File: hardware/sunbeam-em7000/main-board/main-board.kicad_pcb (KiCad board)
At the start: 4 copper layers, 131 x 125 mm, 456 parts, among them J101 TAB1_LINE1, J102 TAB2_LINE_IN, J103 TAB3_NEUTRAL_IN, J106 TAB6_COFVALVE, J107 TAB7_COFFPUMP, J108 TAB8_STEAMPUMP, J109 TAB9_HOTVALVE, J110 WB_RET, J401 SWD, J402 USB_PANEL, J501 TEMP_C, J502 TEMP_S, J503 TEMP_W, J520 FLOW, J521 STM_D, J522 BREW_D, J523 SPARE_A, J524 BREW_A, J525 SPARE_AN2_H, J570 CURR1_H, J571 CURR2_H, J620 PT1_H, J622 PT1_2W_P, J623 PT1_23W_N, J625 PT2_H, J627 PT2_2W_P, J628 PT2_23W_N, J630 WT1_H, J635 WT2_H, J761 WB_LV10, J791 SP2, J821 CON2, J861 KNOB, J862 REED, K201 HF115F-Q/005-1H, K731 HF32FA-G/005-HSL1, K741 HF32FA-G/005-HSL1, Q201 NX3008NBK, Q202 NX3008NBK, Q701 AO3400A, Q711 AO3400A, Q731 AO3400A, Q741 AO3400A, Q761 AO3400A, Q771 AO3400A, Q821 AO3400A, Q822 AO3401A, Q823 AO3400A, Q824 AO3400A, SW401 RESET, T701 BTA204S-600B, T711 BTA204S-600B, U201 74AHCT1G17, U301 IRM-20-5, U302 LT1963AEST-3.3#TRPBF, U401 STM32H743VIT6, U402 TLV803SDBZR, U520 SN74LVC1G17, U601 AMC131M02, U602 LTV-814S-TA1-A, U620 MAX31865ATP+, U621 MAX31865ATP+, U630 HX711, U631 HX711, U701 MOC3052SVM, U711 MOC3052SVM, U791 SN74HCT541PWR, Y401 8 MHz, Y402 32.768 kHz, Y601 8.000MHz

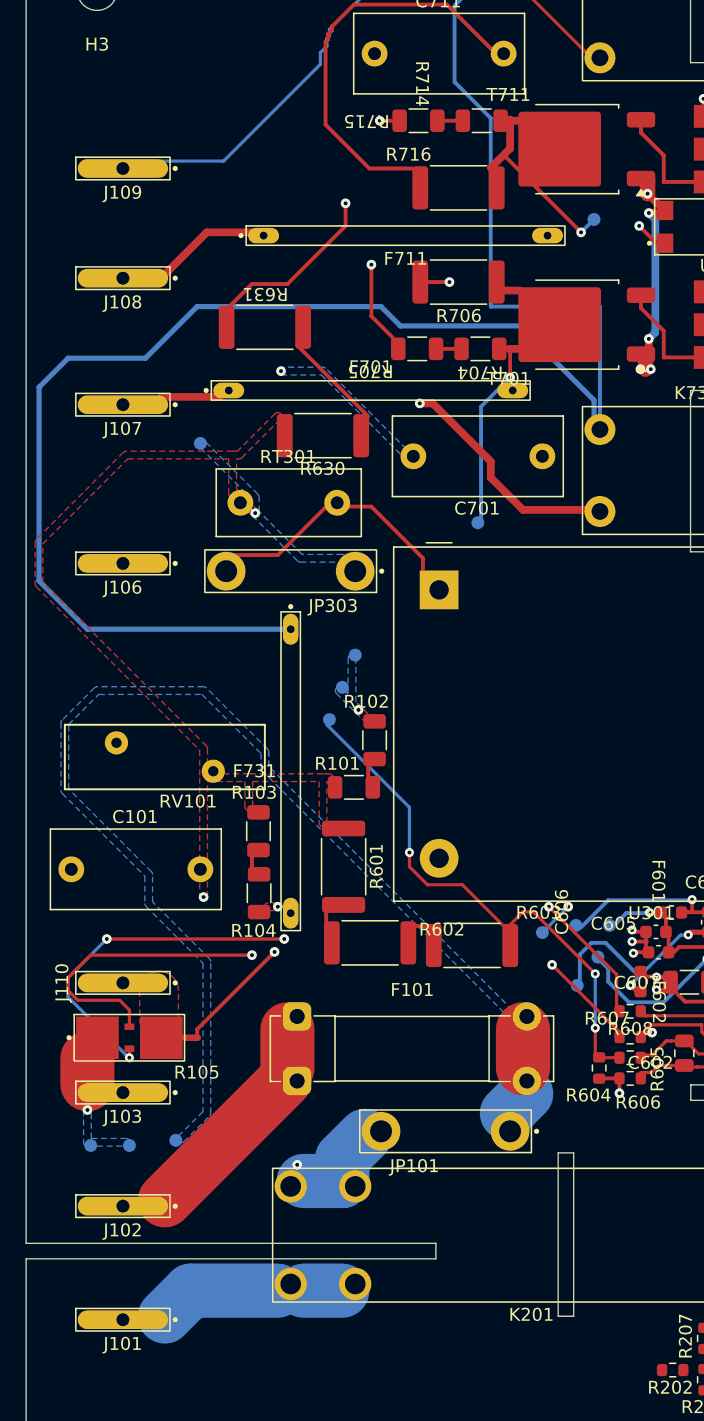
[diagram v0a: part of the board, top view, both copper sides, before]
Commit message: main-board: connect every mains pad the pours left open and fix the mains copper defects found by the early review [SOL-HW-MAIN-BOARD-PROVEN-AND-LAID-OUT.C7]
The NEUTRAL trunk link R105.4-J110.1 (a pour that filled to nothing) is two 3.0 mm tracks with two vias; the triac neutral island, LINE R101/R103, NEUTRAL R102/R104/F731, F711 and the test pads TP101, TP106, TP108 are joined by tracks; LINE1 no longer reaches past the mains region edge; T701 and T711 stand on F.Cu and B.Cu lands; TP105 and TP107 have vias of their own. TP102 stays unconnected (no routable path).

Co-Authored-By: Claude Sonnet 5.5 <noreply@anthropic.com>
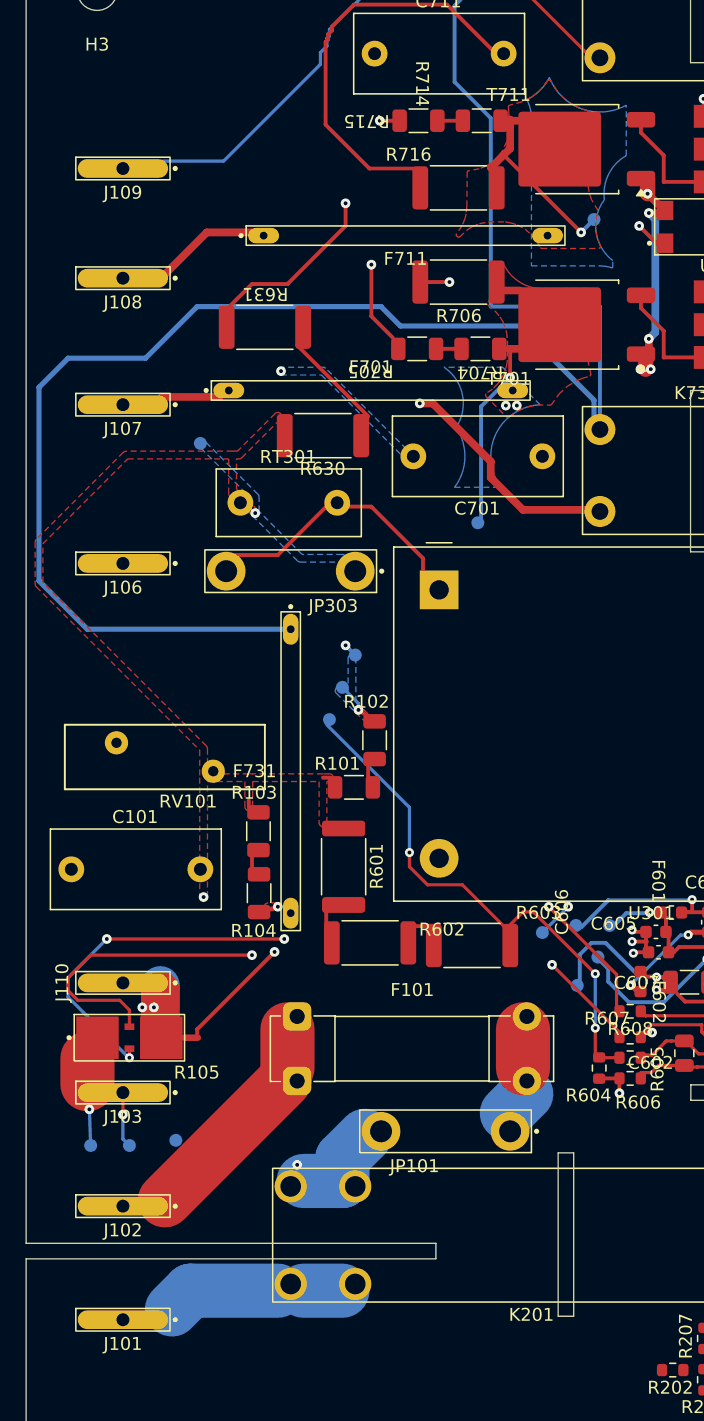
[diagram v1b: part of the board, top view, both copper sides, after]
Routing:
- net /NEUTRAL: track 14.9 -> 46.3 mm, vias 8 -> 11
- net /Mains entry and load feed/NEUTRAL_IN: track 2.00 -> 8.61 mm, vias 1 -> 2
- net /Mains entry and load feed/LINE_IN: track 16.1 -> 21.1 mm
- net /LINE: track 7.22 -> 9.96 mm
- net /LINE1: track 12.6 -> 11.8 mm
- net /Pump drives/PUMP_C_MT2: vias 1 -> 3
- added copper zone on B.Cu, net /Pump drives/PUMP_C_MT2
- added copper zone on F.Cu, net /Pump drives/PUMP_C_MT2
- added copper zone on B.Cu, net /Pump drives/PUMP_S_MT2
- added copper zone on F.Cu, net /Pump drives/PUMP_S_MT2
- removed copper zone on B.Cu, net /Mains entry and load feed/LINE_F
- removed copper zone on B.Cu, net /Mains entry and load feed/NEUTRAL_IN
- removed copper zone on F.Cu, net /Mains entry and load feed/NEUTRAL_IN

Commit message: main-board: move test pads TP102, TP106 and TP108 beside the pads they read and tie each by its own short track [SOL-HW-MAIN-BOARD-PROVEN-AND-LAID-OUT.C7]
TP102 (LINE_F) was in a closed B.Cu pocket no copper could reach within the signed figures; it now stands beside F101's load clip at (42.0, 93.0) on a 1.7 mm track to the LINE_F copper at JP101 pin 1. TP106 and TP108 (NEUTRAL) stood 30.6 and 32.7 mm from R105 pad 4; they now stand at (15.5, 80.0) and (15.5, 82.5) on their own short tracks to the B.Cu NEUTRAL copper that joins pad 4 to J110 pin 1. Their long tracks and the via at (25.75, 56.25) are removed; the via at (26.75, 61.25) stays, it joins R102 pin 2. hw:placement LENGTH 9162.3832 -> 9138.6764 mm, CROSSINGS 3340 -> 3336. The board was refilled and saved twice and compared identical; the five critical classes locked again (4 items locked now, 478 already). Own connectivity check: only the 173 open ground components of stage 2 remain.

Co-Authored-By: Claude Sonnet 5.5 <noreply@anthropic.com>
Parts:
- moved TP102 29.4 mm to (42.0, 93.0)
- moved TP108 27.8 mm to (15.5, 82.5)
- moved TP106 22.8 mm to (15.5, 80.0)
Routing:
- net /NEUTRAL: track 46.3 -> 50.6 mm, vias 11 -> 10
- net /Mains entry and load feed/LINE_F: track 5.12 -> 6.82 mm
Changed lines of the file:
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@@
 	(footprint "main-board:TestPoint_Pad_D1.0mm_Tight"
 		(layer "B.Cu")
-		(at 25.5013 59.5 180)
+		(at 15.5 80 180)
 		(descr "SMD pad as test point, diameter 1.0 mm, courtyard 0.25 mm beyond the copper so test points can stand 2.5 mm apart and still keep the 1 mm test-point-to-courtyard distance")
 		(tags "test point SMD pad")
 		(property "Reference" "TP106"
-			(at 1.95 1.45 0)
+			(at 0 1.45 0)
 			(unlocked yes)
 			(layer "B.SilkS")
@@
 	(footprint "main-board:TestPoint_Pad_D1.0mm_Tight"
 		(layer "B.Cu")
-		(at 26.5013 57 180)
+		(at 15.5 82.5 180)
 		(descr "SMD pad as test point, diameter 1.0 mm, courtyard 0.25 mm beyond the copper so test points can stand 2.5 mm apart and still keep the 1 mm test-point-to-courtyard distance")
 		(tags "test point SMD pad")
 		(property "Reference" "TP108"
-			(at 0.05 1.45 0)
+			(at 0 -1.45 0)
 			(unlocked yes)
 			(layer "B.SilkS")
@@
 	(footprint "main-board:TestPoint_Pad_D1.0mm_Tight"
 		(layer "B.Cu")
-		(at 12.6 94.6 180)
+		(at 42 93 180)
 		(descr "SMD pad as test point, diameter 1.0 mm, courtyard 0.25 mm beyond the copper so test points can stand 2.5 mm apart and still keep the 1 mm test-point-to-courtyard distance")
 		(tags "test point SMD pad")
 		(property "Reference" "TP102"
-			(at -0.05 1.45 0)
+			(at -3.5 0 0)
 			(unlocked yes)
 			(layer "B.SilkS")
@@
 	)
 	(via
-		(at 25.75 56.25)
-		(size 0.75)
-		(drill 0.3)
-		(layers "F.Cu" "B.Cu")
-		(locked yes)
-		(net "/NEUTRAL")
-	)
-	(via
 		(at 49.4 34.85)
 		(size 0.75)
@@
 	)
 	(segment
-		(start 25.5 59.5)
-		(end 26.75 60.75)
-		(width 0.25)
+		(start 49.25 32.5)
+		(end 49.75 32)
+		(width 0.6)
 		(locked yes)
 		(layer "B.Cu")
@@
 	)
 	(segment
-		(start 26.25 56.75)
-		(end 25.75 56.25)
-		(width 0.3)
+		(start 13.4 80)
+		(end 12 81.4)
+		(width 0.25)
 		(locked yes)
 		(layer "B.Cu")
@@
 	)
 	(segment
-		(start 49.25 32.5)
-		(end 49.75 32)
-		(width 0.6)
+		(start 15.5 80)
+		(end 13.4 80)
+		(width 0.25)
 		(locked yes)
 		(layer "B.Cu")
@@
 	)
 	(segment
-		(start 26.75 60.75)
-		(end 26.75 61.25)
-		(width 0.25)
+		(start 49.75 23.25)
+		(end 49.25 22.75)
+		(width 0.6)
 		(locked yes)
 		(layer "B.Cu")
@@
 	)
 	(segment
-		(start 49.75 23.25)
-		(end 49.25 22.75)
-		(width 0.6)
+		(start 15.5 82.5)
+		(end 12.3 82.5)
+		(width 0.25)
 		(locked yes)
 		(layer "B.Cu")
@@
 	)
 	(segment
-		(start 25.75 56.25)
-		(end 25.75 56.25)
-		(width 0.3)
-		(locked yes)
-		(layer "In2.Cu")
-		(net "/NEUTRAL")
-	)
-	(segment
 		(start 32.25 78)
 		(end 31 78)
@@
 		(locked yes)
 		(layer "B.Cu")
+		(net "/Mains entry and load feed/LINE_F")
+	)
+	(segment
+		(start 42 93)
+		(end 40.3 93)
+		(width 0.25)
+		(locked yes)
+		(layer "B.Cu")

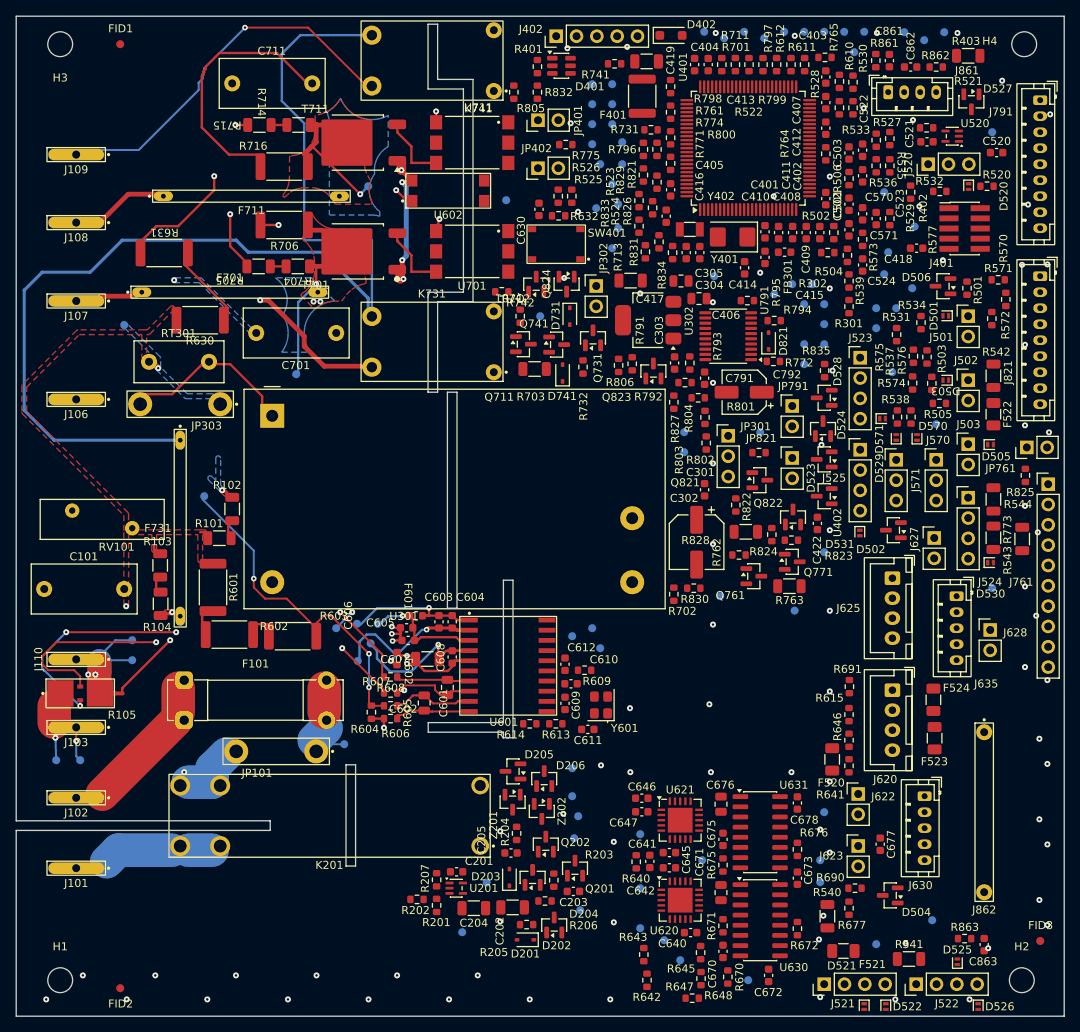
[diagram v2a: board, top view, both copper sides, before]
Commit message: main-board: ground vias beside every GND pad, GND pours on F.Cu and B.Cu, stitching [SOL-HW-MAIN-BOARD-PROVEN-AND-LAID-OUT.C7]
Co-Authored-By: Claude Sonnet 5.5 <noreply@anthropic.com>
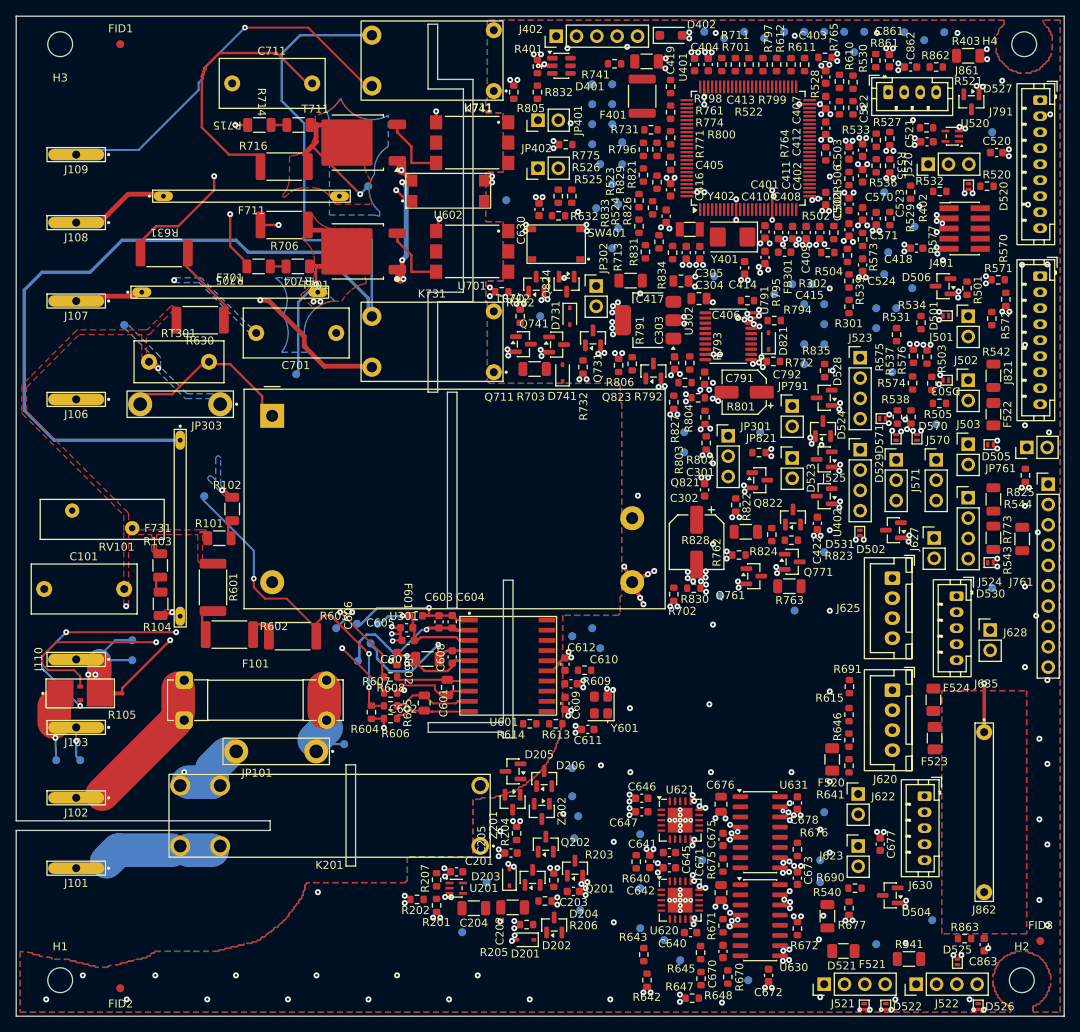
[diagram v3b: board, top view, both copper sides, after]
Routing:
- net GND: track 0.00 -> 25.4 mm, vias 83 -> 454
- added copper zone on B.Cu, net GND
- added copper zone on F.Cu, net GND

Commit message: main-board: Supply5V distribution (+5V, +5V_MOD, +5V_WB, +5V_GAUGE, USB_VBUS_F) at the class widths [SOL-HW-MAIN-BOARD-PROVEN-AND-LAID-OUT.C7]
Co-Authored-By: Claude Sonnet 5.5 <noreply@anthropic.com>
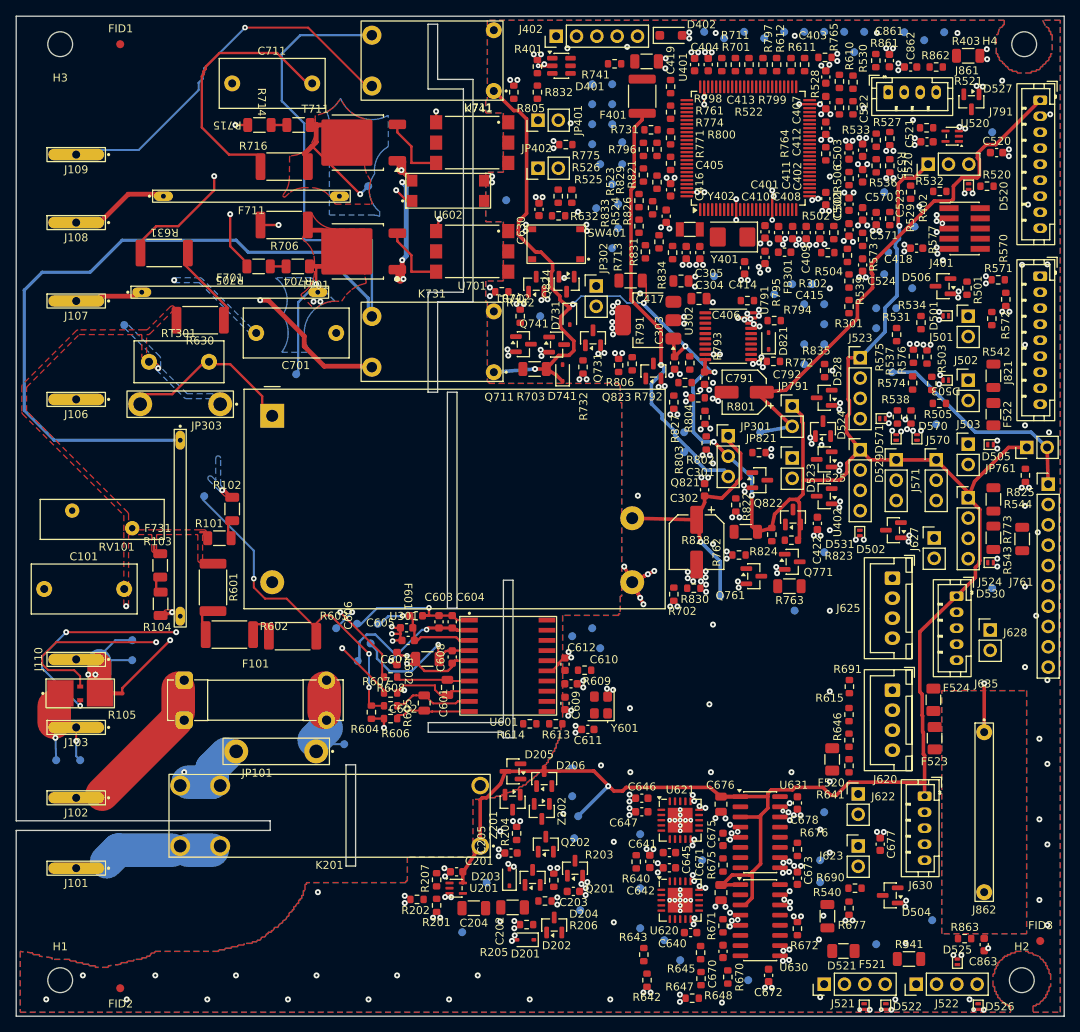
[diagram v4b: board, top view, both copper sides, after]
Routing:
- net +5V: track 0.00 -> 361.3 mm, vias 0 -> 9
- net +5V_GAUGE: track 0.00 -> 65.8 mm
- net /USB_VBUS_F: track 0.00 -> 53.4 mm, vias 0 -> 1
- net /Logic supply/+5V_MOD: track 0.00 -> 33.4 mm, vias 0 -> 1
- net +5V_WB: track 0.00 -> 27.8 mm
